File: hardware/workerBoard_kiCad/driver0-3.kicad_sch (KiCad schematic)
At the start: 41 parts, among them J1 1053141216, U10 ADA4841-2YRMZ-RL, U7 ADA4841-2YRMZ-RL, U8 ADA4841-2YRMZ-RL, U9 ADA4841-2YRMZ-RL

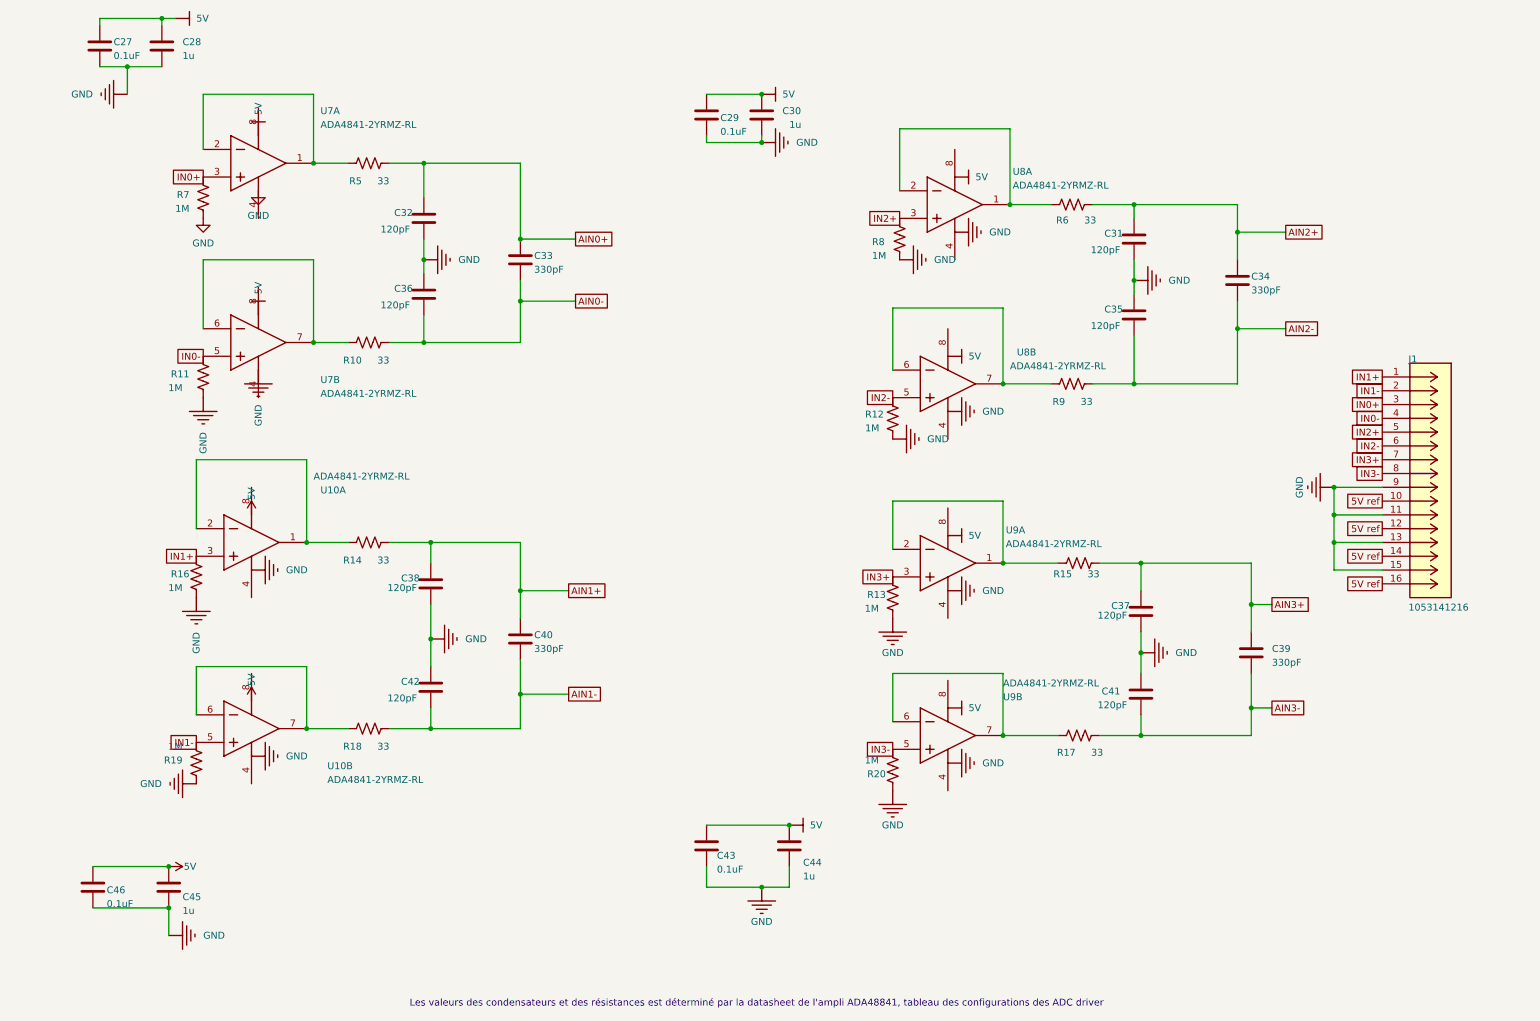
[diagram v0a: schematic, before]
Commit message: changed the symbol for the op amp in the driver schematic
Changed the symbol for the ADA4841
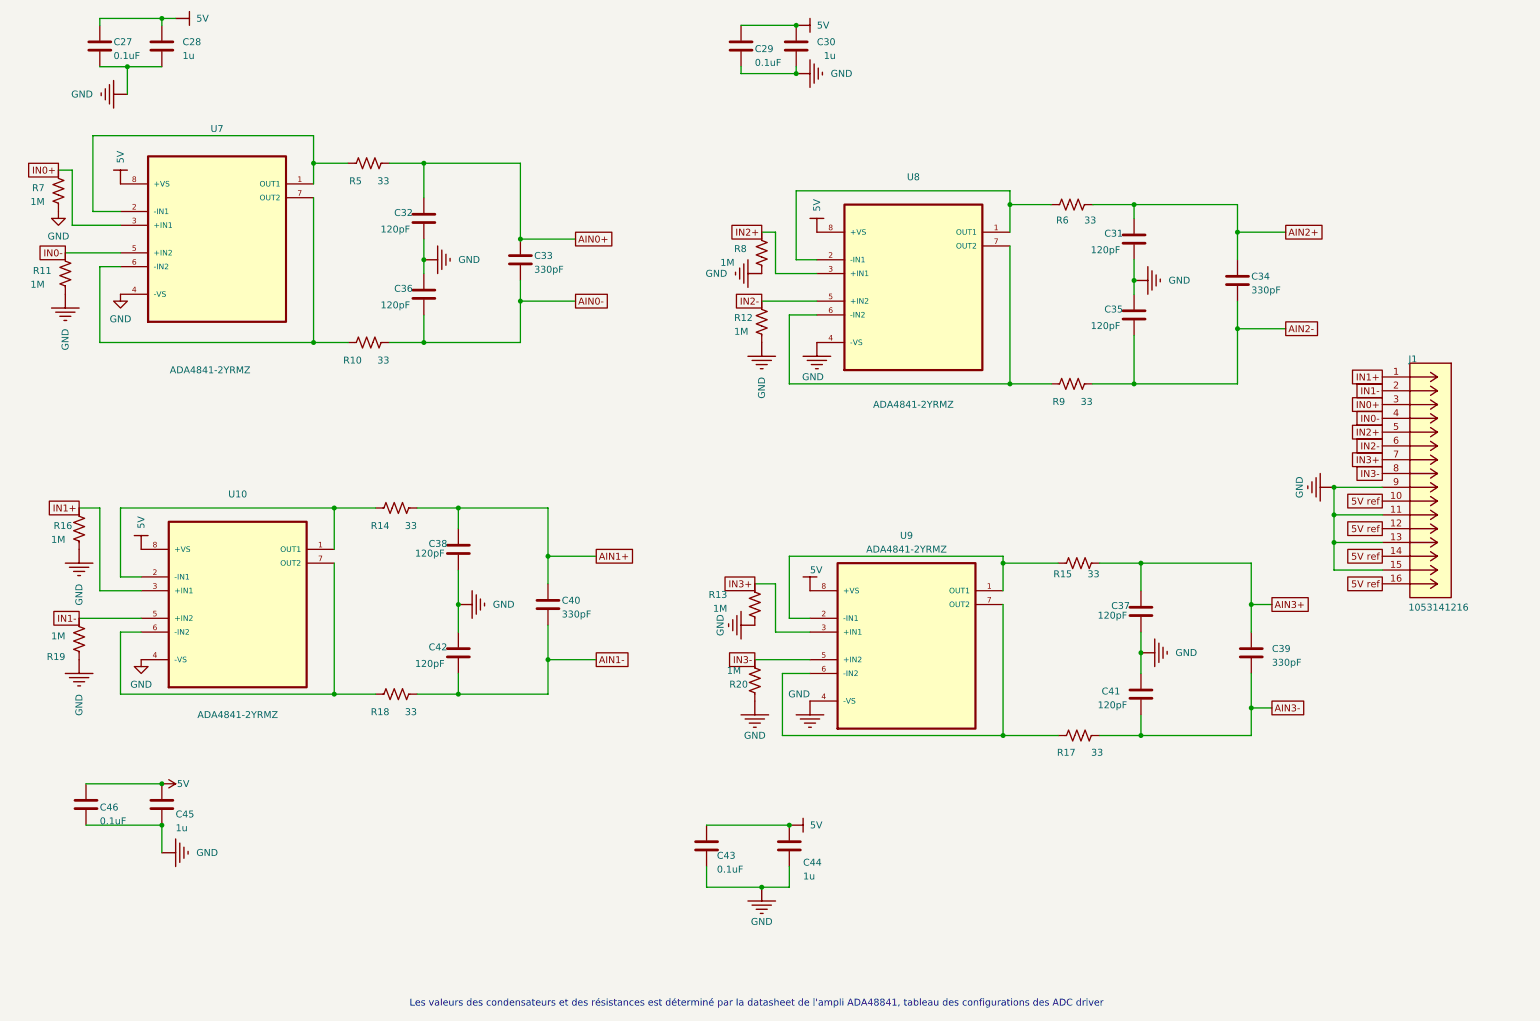
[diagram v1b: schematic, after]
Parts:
- removed U10, U7, U8, U9: ADA4841-2YRMZ-RL, lib:ADI-RM-8_M, symbol ADA4841_2:ADA4841_B
- added U10, U7, U8, U9: ADA4841-2YRMZ, bib:ADI-RM-8_M, symbol ADA4841:ADA4841-2YRMZ
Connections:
- net 5V: now also U10.8 (+VS), U7.8 (+VS), U8.8 (+VS), U9.8 (+VS)
- net GND: now also U10.4 (-VS), U7.4 (-VS), U8.4 (-VS), U9.4 (-VS)
- net IN0+: now also U7.3 (+IN1)
- net IN0-: now also U7.5 (+IN2)
- net IN1+: now also U10.3 (+IN1)
- net IN1-: now also U10.5 (+IN2)
- net IN2+: now also U8.3 (+IN1)
- net IN2-: now also U8.5 (+IN2)
- net IN3+: now also U9.3 (+IN1)
- net IN3-: now also U9.5 (+IN2)
- net at R10.1: now also U7.6 (-IN2), U7.7 (OUT2)
- net at R18.1: now also U10.6 (-IN2), U10.7 (OUT2)
- net at R17.1: now also U9.6 (-IN2), U9.7 (OUT2)
- net at R14.1: now also U10.1 (OUT1), U10.2 (-IN1)
- net at R9.1: now also U8.6 (-IN2), U8.7 (OUT2)
- net at R15.1: now also U9.1 (OUT1), U9.2 (-IN1)
- net at R5.1: now also U7.1 (OUT1), U7.2 (-IN1)
- net at R6.1: now also U8.1 (OUT1), U8.2 (-IN1)
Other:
- moved on the sheet: C29, C30, C38, C40, C42, C45, C46, R11, R12, R13, R14, R16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

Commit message: DRC clean
Remove the warning by repositioning the label on both top and bottom layer
Replace the +5V net for the 5V net
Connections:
- net +5V is gone; now on net 5V: C45.1, C46.1
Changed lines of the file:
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@@
   (junction (at 67.31 77.47) (diameter 0) (color 0 0 0 0)
   )
+  (junction (at 194.31 118.11) (diameter 0) (color 0 0 0 0)
+  )
+  (junction (at 93.98 107.95) (diameter 0) (color 0 0 0 0)
+  )
+  (junction (at 218.44 66.04) (diameter 0) (color 0 0 0 0)
+  )
+  (junction (at 219.71 118.11) (diameter 0) (color 0 0 0 0)
+  )
+  (junction (at 255.27 109.22) (diameter 0) (color 0 0 0 0)
+  )
+  (junction (at 237.49 57.15) (diameter 0) (color 0 0 0 0)
+  )
   (junction (at 39.37 158.75) (diameter 0) (color 0 0 0 0)
-  )
-  (junction (at 194.31 118.11) (diameter 0) (color 0 0 0 0)
-  )
-  (junction (at 93.98 107.95) (diameter 0) (color 0 0 0 0)
-  )
-  (junction (at 218.44 66.04) (diameter 0) (color 0 0 0 0)
-  )
-  (junction (at 219.71 118.11) (diameter 0) (color 0 0 0 0)
-  )
-  (junction (at 255.27 109.22) (diameter 0) (color 0 0 0 0)
-  )
-  (junction (at 237.49 57.15) (diameter 0) (color 0 0 0 0)
   )
   (junction (at 93.98 142.24) (diameter 0) (color 0 0 0 0)
@@
     (pin "2")
   )
+  (symbol (lib_id "driver0-3-altium-import:5V") (at 39.37 158.75 180) (unit 1)
+    (in_bom yes) (on_board yes)
+    (property "Reference" "#PWR?" (id 0) (at 39.37 158.75 0)
+      (effects (font (size 1.27 1.27)) hide)
+    )
+    (property "Value" "5V" (id 1) (at 39.37 154.94 90)
+      (effects (font (size 1.27 1.27)) (justify right))
+    )
+    (property "Footprint" "" (id 2) (at 39.37 158.75 0)
+      (effects (font (size 1.27 1.27)) hide)
+    )
+    (property "Datasheet" "" (id 3) (at 39.37 158.75 0)
+      (effects (font (size 1.27 1.27)) hide)
+    )
+    (pin "")
+  )
   (symbol (lib_id "Device:C") (at 39.37 162.56 0) (unit 1)
     (in_bom yes) (on_board yes)
@@
     (pin "2")
   )
-  (symbol (lib_id "power:+5V") (at 39.37 158.75 270) (unit 1)
-    (in_bom yes) (on_board yes)
-    (property "Reference" "#PWR0142" (id 0) (at 39.37 158.75 0)
-      (effects (font (size 1.27 1.27)) hide)
-    )
-    (property "Value" "5V" (id 1) (at 44.45 158.75 90)
-      (effects (font (size 1.27 1.27)) (justify right))
-    )
-    (property "Footprint" "" (id 2) (at 39.37 158.75 0)
-      (effects (font (size 1.27 1.27)) hide)
-    )
-    (property "Datasheet" "" (id 3) (at 39.37 158.75 0)
-      (effects (font (size 1.27 1.27)) hide)
-    )
-    (pin "1")
-  )
   (symbol (lib_id "Device:C") (at 156.21 22.86 0) (unit 1)

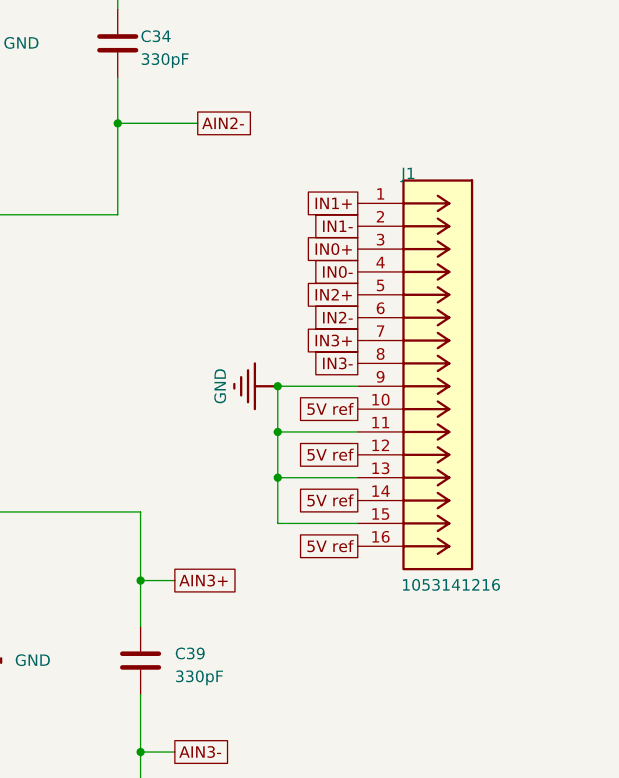
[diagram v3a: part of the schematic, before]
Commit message: Changed worker board layout V2
Removed micro-vias, used only two layers, changed connectors and generally re-worked the worker board
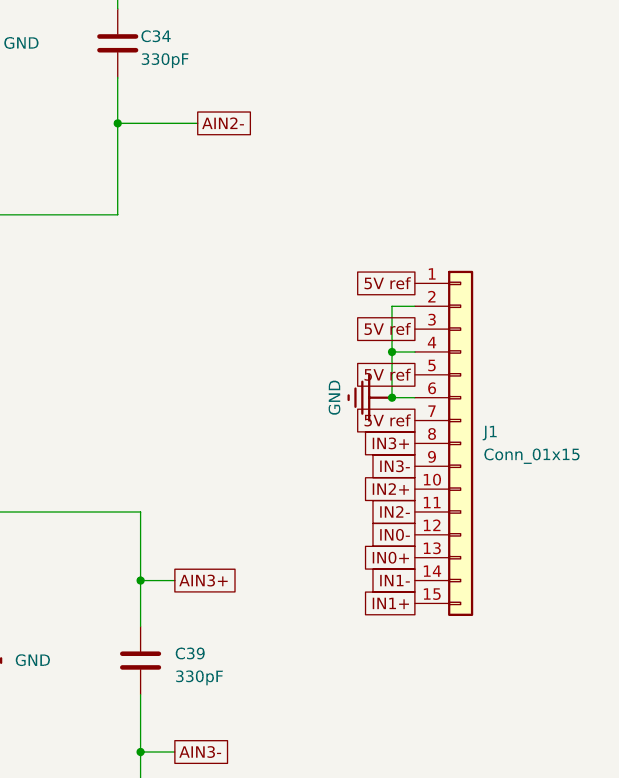
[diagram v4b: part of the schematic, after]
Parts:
- removed J1: 1053141216, lib:CON_1053141216, symbol lib:connector_accel
- added J1: Conn_01x15, Connector_Molex:Molex_Pico-Clasp_202396-1507_1x15-1MP_P1.00mm_Horizontal, symbol Connector_Generic:Conn_01x15
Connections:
- net 5V ref: now also J1.1 (Pin_1), J1.3 (Pin_3), J1.5 (Pin_5), J1.7 (Pin_7)
- net GND: now also J1.2 (Pin_2), J1.4 (Pin_4), J1.6 (Pin_6)
- net IN0+: now also J1.13 (Pin_13)
- net IN0-: now also J1.12 (Pin_12)
- net IN1+: now also J1.15 (Pin_15)
- net IN1-: now also J1.14 (Pin_14)
- net IN2+: now also J1.10 (Pin_10)
- net IN2-: now also J1.11 (Pin_11)
- net IN3+: now also J1.8 (Pin_8)
- net IN3-: now also J1.9 (Pin_9)

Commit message: Fixed DRC violations
Fixed DRC violations based on missing footprints. Should review THVD8000 foot print as it had to be changed from 'missing' footprint import. This version passes all DRC checks. Net clearance was changed to 0.127 mm (4mill) otherwise the SOT-23 pads were failling DRC
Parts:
- renumbered C46 to C14, C27 to C15, C28 to C16, C45 to C17, C32 to C18, C36 to C19, C38 to C20, C42 to C21, C33 to C22, C40 to C23, C43 to C24, C29 to C25, C44 to C26, C30 to C27, C31 to C28, C35 to C29, C37 to C30, C41 to C31, C34 to C32, C39 to C33, J1 to J4, R13 to R10, R20 to R11, R8 to R12, R12 to R13, R6 to R14, R9 to R15, R15 to R16, R7 to R2, R11 to R3, R16 to R4, R19 to R5, R5 to R6, R10 to R7, R14 to R8, R18 to R9, U7 to U3, U10 to U4, U9 to U5, U8 to U6
